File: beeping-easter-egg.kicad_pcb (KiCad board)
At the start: 2 copper layers, 9 parts, among them Q1 2N3904, SW1 SW_SPDT_312, U1 ICM7556

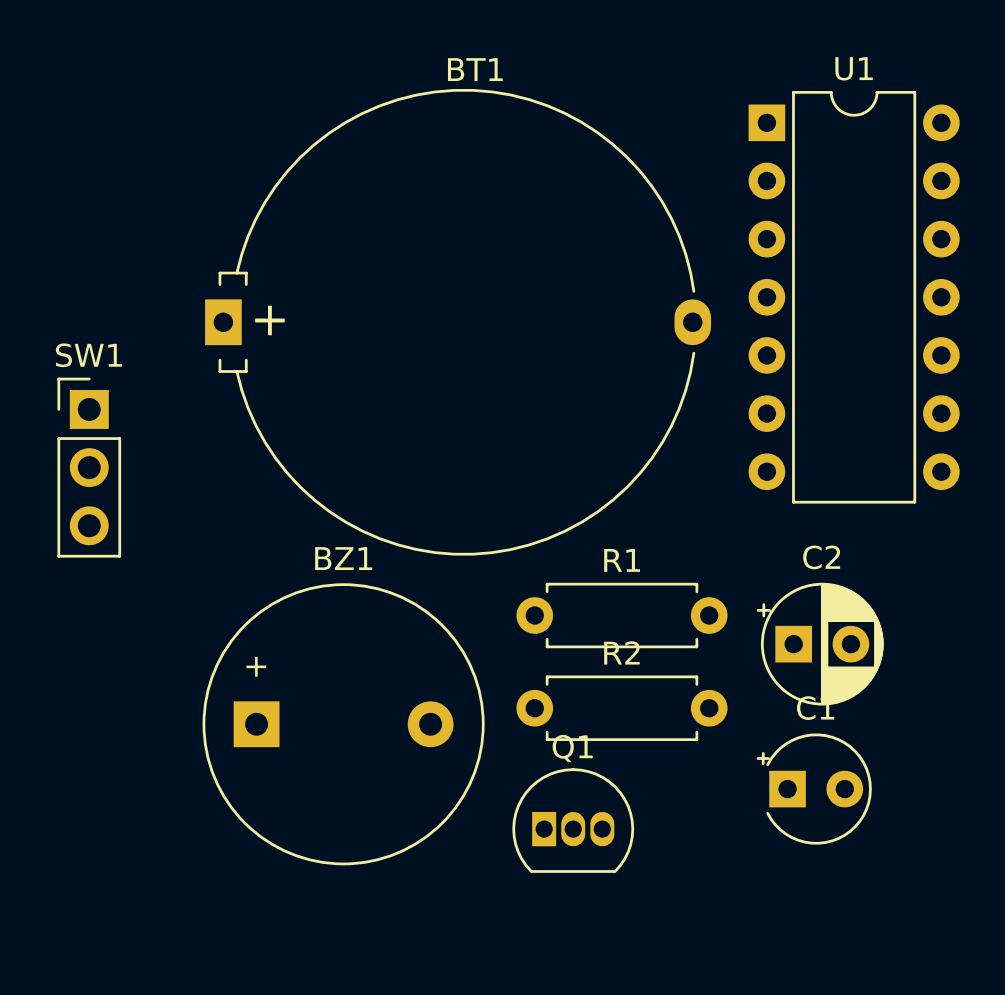
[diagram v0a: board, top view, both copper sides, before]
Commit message: update pcb from schematic
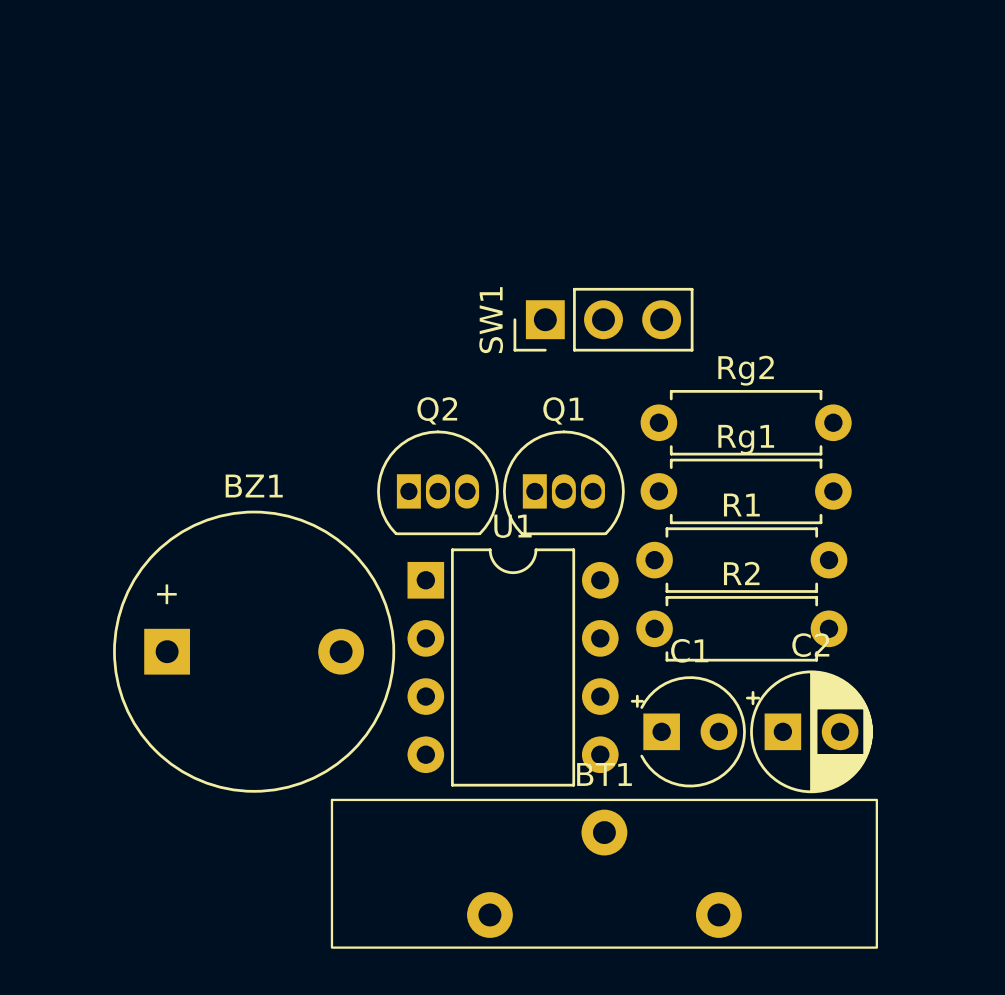
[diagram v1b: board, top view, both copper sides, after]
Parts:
- added Q2: 2N3906, Package_TO_SOT_THT:TO-92_Inline, F.Cu at (142.5, 84.0)
- added Rg1: 10kΩ, Resistor_THT:R_Axial_DIN0207_L6.3mm_D2.5mm_P7.62mm_Horizontal, F.Cu at (153.4, 84.0)
- added Rg2: 220Ω, Resistor_THT:R_Axial_DIN0207_L6.3mm_D2.5mm_P7.62mm_Horizontal, F.Cu at (153.4, 81.0)
- BT1: footprint Battery:Battery_Panasonic_CR2032-HFN_Horizontal_CircularHoles -> Library:AAA-BAT-038-K01
- C1: value C -> 10nF
- C2: value C_Polarized_US -> 0.47µF
- Q1: value 2N3904 -> 2N3906
- R1: renamed from R2; value R_US -> 510kΩ
- R2: renamed from R1; value R_US -> 1MΩ
- U1: value ICM7556 -> TLC555xP; footprint Package_DIP:DIP-14_W7.62mm -> Package_DIP:DIP-8_W7.62mm
- moved BT1 29.3 mm to (151.0, 100.7)
- moved U1 24.9 mm to (143.2, 87.9)
- moved SW1 20.3 mm to (148.4, 76.5), turned to 90 degrees
- moved Q1 14.8 mm to (148.0, 84.0)
- moved R1 8.32 mm to (153.2, 87.0)
- moved C1 6.04 mm to (153.5, 94.5)
- moved R2 5.26 mm to (153.2, 90.0)
- moved BZ1 5.03 mm to (131.9, 91.0)
- moved C2 3.86 mm to (158.8, 94.5)
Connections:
- BZ1 pad 2: Net-(BZ1--) -> Net-(BT1--)
- C1 pad 1: Net-(U1A-CV) -> Net-(U1-CV)
- C2 pad 1: Net-(U1A-THR) -> Net-(U1-THR)
- Q1 pad 1: Net-(BT1--) -> Net-(Q1-E)
- Q1 pad 3: Net-(BZ1--) -> Net-(Q1-C)
- R1 pad 1: Net-(U1A-THR) -> Net-(Q1-C)
- R1 pad 2: Net-(U1A-DIS) -> Net-(U1-DIS)
- R2 pad 1: Net-(BZ1-+) -> Net-(U1-DIS)
- R2 pad 2: Net-(U1A-DIS) -> Net-(U1-THR)
- SW1 pad 3: Net-(BZ1-+) -> Net-(Q1-E)
- U1 pad 1: Net-(U1A-DIS) -> Net-(BT1--)
- U1 pad 2: Net-(U1A-THR) -> Net-(U1-THR)
- U1 pad 3: Net-(U1A-CV) -> Net-(U1-Q)
- U1 pad 4: Net-(BZ1-+) -> Net-(Q1-C)
- U1 pad 5: Net-(U1A-Q) -> Net-(U1-CV)
- U1 pad 6: Net-(U1A-THR) -> Net-(U1-THR)
- U1 pad 7: Net-(BT1--) -> Net-(U1-DIS)
- U1 pad 8: Net-(U1A-Q) -> Net-(Q1-C)

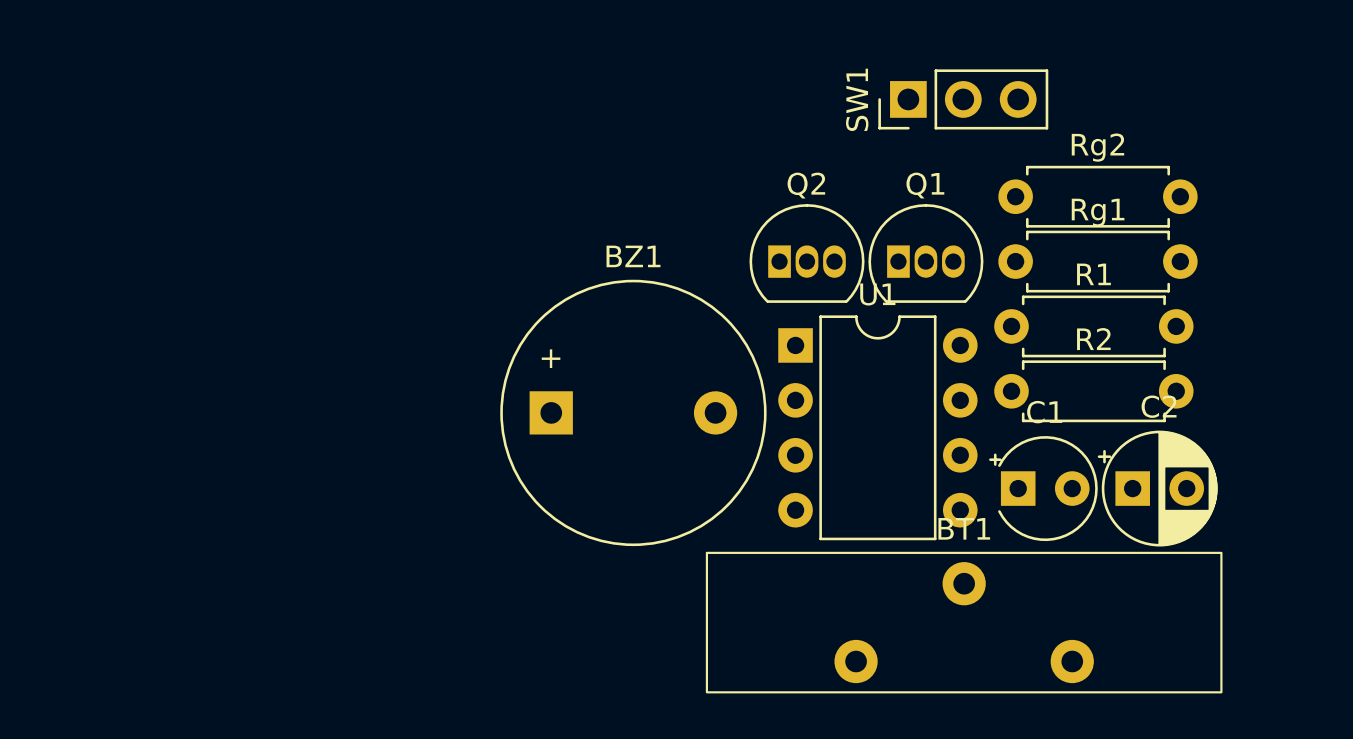
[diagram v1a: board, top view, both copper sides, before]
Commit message: switch from bjts to mosfets
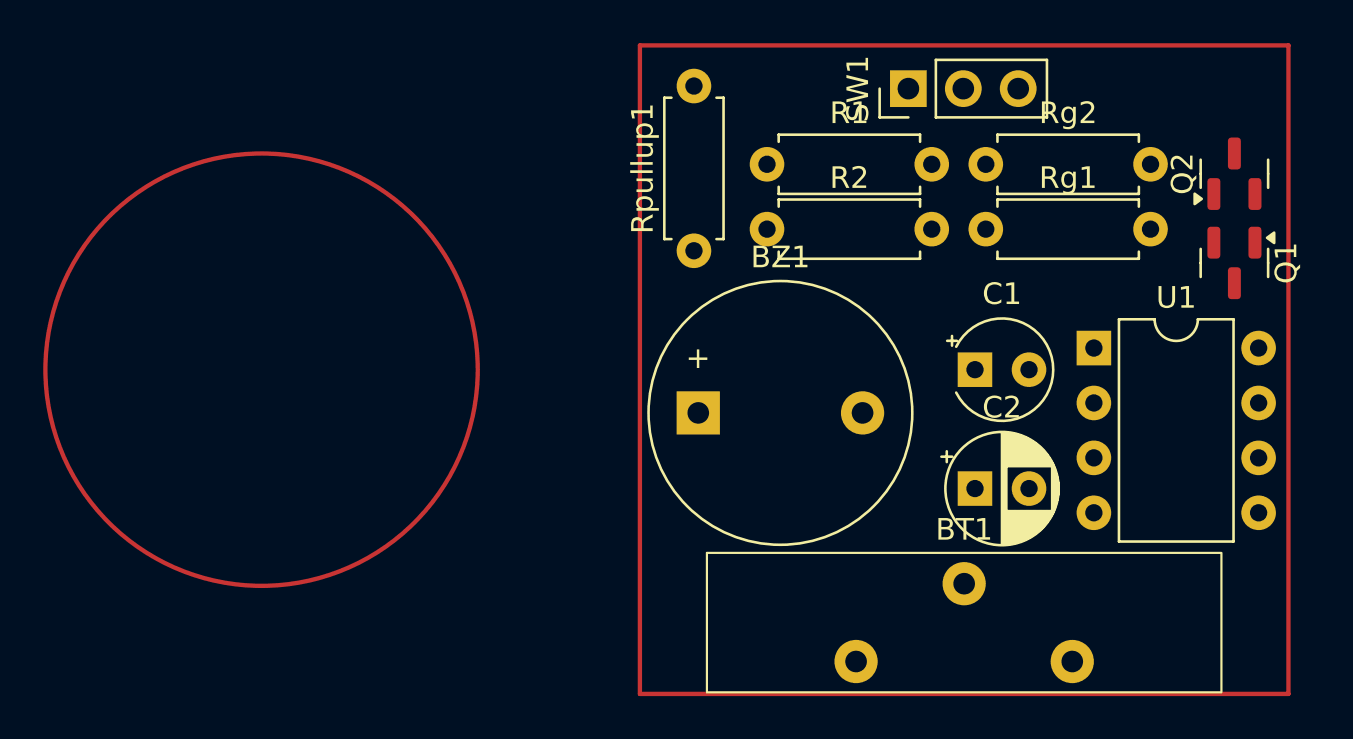
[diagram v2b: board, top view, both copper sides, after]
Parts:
- added Rpullup1: 10kΩ, Resistor_THT:R_Axial_DIN0207_L6.3mm_D2.5mm_P7.62mm_Horizontal, F.Cu at (138.5, 83.5)
- Q1, Q2: value 2N3906 -> AO3401A; footprint Package_TO_SOT_THT:TO-92_Inline -> Package_TO_SOT_SMD:SOT-23
- Rg1: value 10kΩ -> 100Ω
- Rg2: value 220Ω -> 100Ω
- moved Q2 21.4 mm to (163.5, 79.9), turned to 90 degrees
- moved Q1 15.5 mm to (163.5, 84.1), turned to -90 degrees
- moved U1 13.8 mm to (157.0, 88.0)
- moved R1 13.6 mm to (141.9, 79.5)
- moved R2 13.6 mm to (141.9, 82.5)
- moved C2 7.29 mm to (151.5, 94.5)
- moved BZ1 6.80 mm to (138.7, 91.0)
- moved C1 5.85 mm to (151.5, 89.0)
- moved Rg1 2.04 mm to (152.0, 82.5)
- moved Rg2 2.04 mm to (152.0, 79.5)
- moved SW1 0.50 mm to (148.4, 76.0)
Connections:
- Q1 pad 1: Net-(Q1-E) -> Net-(Q1-G)
- Q1 pad 2: Net-(Q1-B) -> Net-(Q1-S)
- Q1 pad 3: Net-(Q1-C) -> Net-(Q1-D)
- Q2 pad 1: Net-(Q1-C) -> Net-(Q2-G)
- Q2 pad 2: Net-(Q2-B) -> Net-(Q1-S)
- R1 pad 1: Net-(Q1-C) -> Net-(Q1-S)
- Rg1 pad 1: Net-(Q1-B) -> Net-(Q1-G)
- Rg2 pad 1: Net-(Q2-B) -> Net-(Q2-G)
- SW1 pad 3: Net-(Q1-E) -> Net-(Q1-D)
- U1 pad 4: Net-(Q1-C) -> Net-(Q1-S)
- U1 pad 8: Net-(Q1-C) -> Net-(Q1-S)

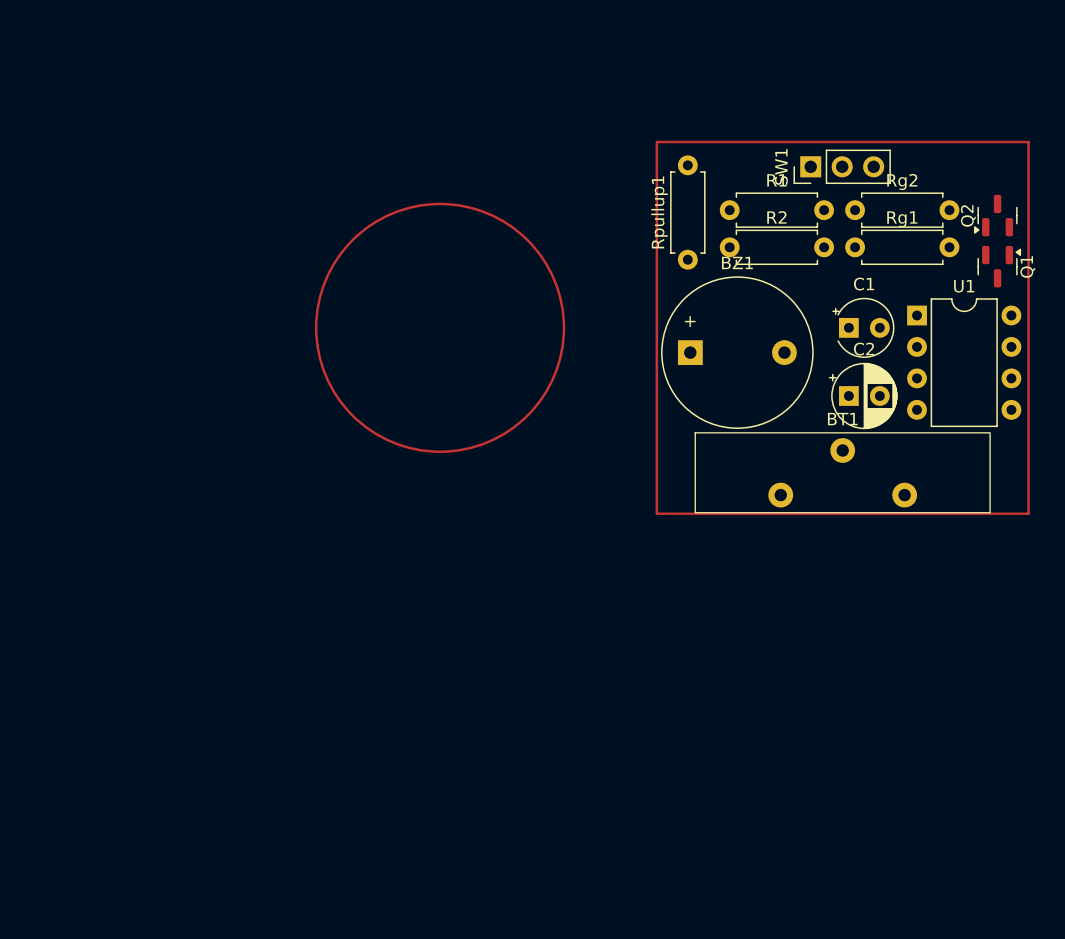
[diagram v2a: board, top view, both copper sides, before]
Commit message: Switch to SMD footprints. Add filter cap to reset.
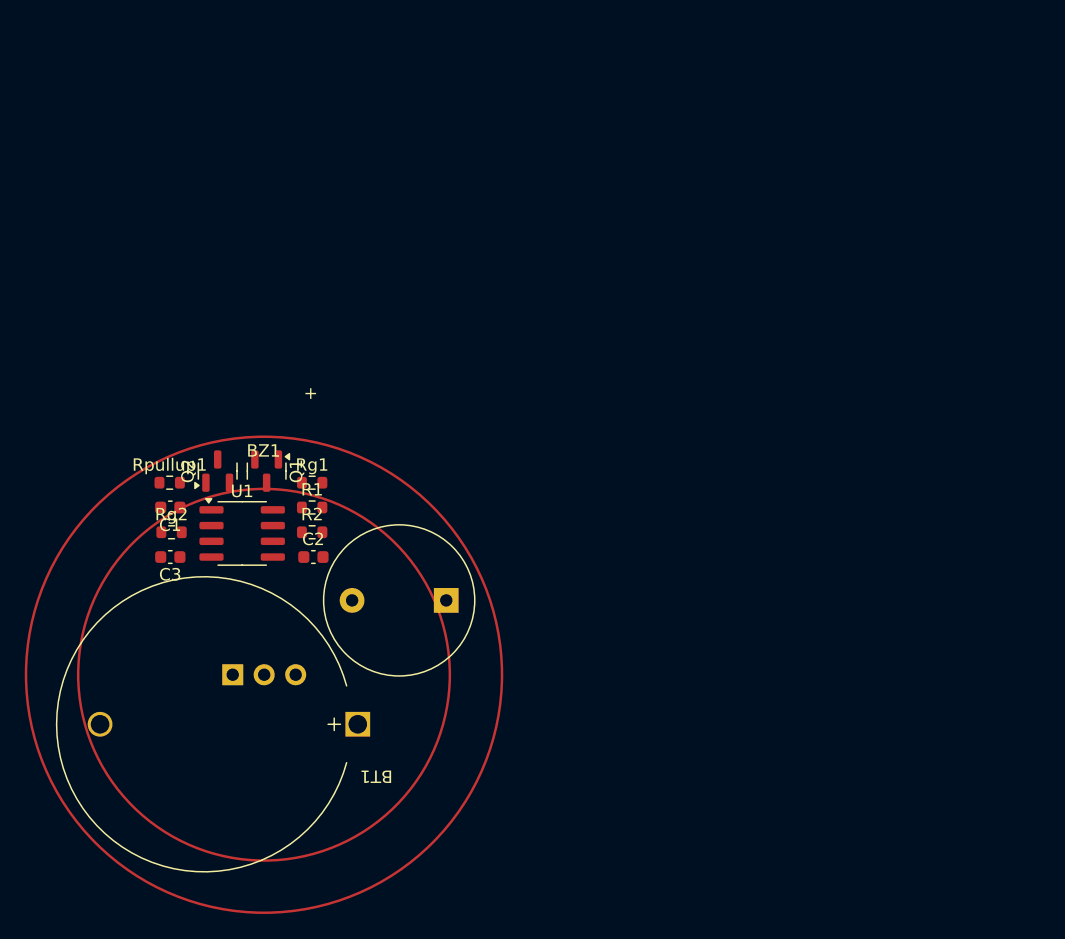
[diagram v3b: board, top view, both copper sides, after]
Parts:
- added C3: 10nF, Capacitor_SMD:C_0603_1608Metric, F.Cu at (96.7, 107.5)
- BT1: footprint Library:AAA-BAT-038-K01 -> Battery:BatteryHolder_MYOUNG_BS-07-A1BJ001_CR2032
- C1: value 10nF -> 0.47µF; footprint Capacitor_THT:CP_Radial_Tantal_D4.5mm_P2.50mm -> Capacitor_SMD:C_0603_1608Metric
- C2: value 0.47µF -> 10nF; footprint Capacitor_THT:CP_Radial_D5.0mm_P2.50mm -> Capacitor_SMD:C_0603_1608Metric
- R1, R2, Rg1, Rpullup1: footprint Resistor_THT:R_Axial_DIN0207_L6.3mm_D2.5mm_P7.62mm_Horizontal -> Resistor_SMD:R_0603_1608Metric
- Rg2: value 100Ω -> 300Ω; footprint Resistor_THT:R_Axial_DIN0207_L6.3mm_D2.5mm_P7.62mm_Horizontal -> Resistor_SMD:R_0603_1608Metric
- SW1: moved to B.Cu
- U1: footprint Package_DIP:DIP-8_W7.62mm -> Package_SO:SOIC-8_3.9x4.9mm_P1.27mm
- moved Q2 66.2 mm to (100.5, 100.6)
- moved SW1 62.1 mm to (101.8, 117.0), turned to -90 degrees
- moved Q1 61.3 mm to (104.5, 100.6)
- moved Rg2 61.0 mm to (96.8, 105.5)
- moved U1 57.2 mm to (102.5, 105.6)
- moved C1 56.7 mm to (96.7, 103.5), turned to 180 degrees
- moved Rg1 47.8 mm to (108.2, 101.5)
- moved Rpullup1 45.5 mm to (96.7, 101.5), turned to 0 degrees
- moved C2 45.1 mm to (108.3, 107.5)
- moved BT1 44.1 mm to (111.9, 121.0), turned to 180 degrees
- moved R1 41.4 mm to (108.2, 103.5)
- moved R2 40.8 mm to (108.2, 105.5)
- moved BZ1 28.1 mm to (119.0, 111.0), turned to 180 degrees
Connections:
- C1 pad 1: Net-(U1-CV) -> Net-(U1-THR)
- C2 pad 1: Net-(U1-THR) -> Net-(U1-CV)

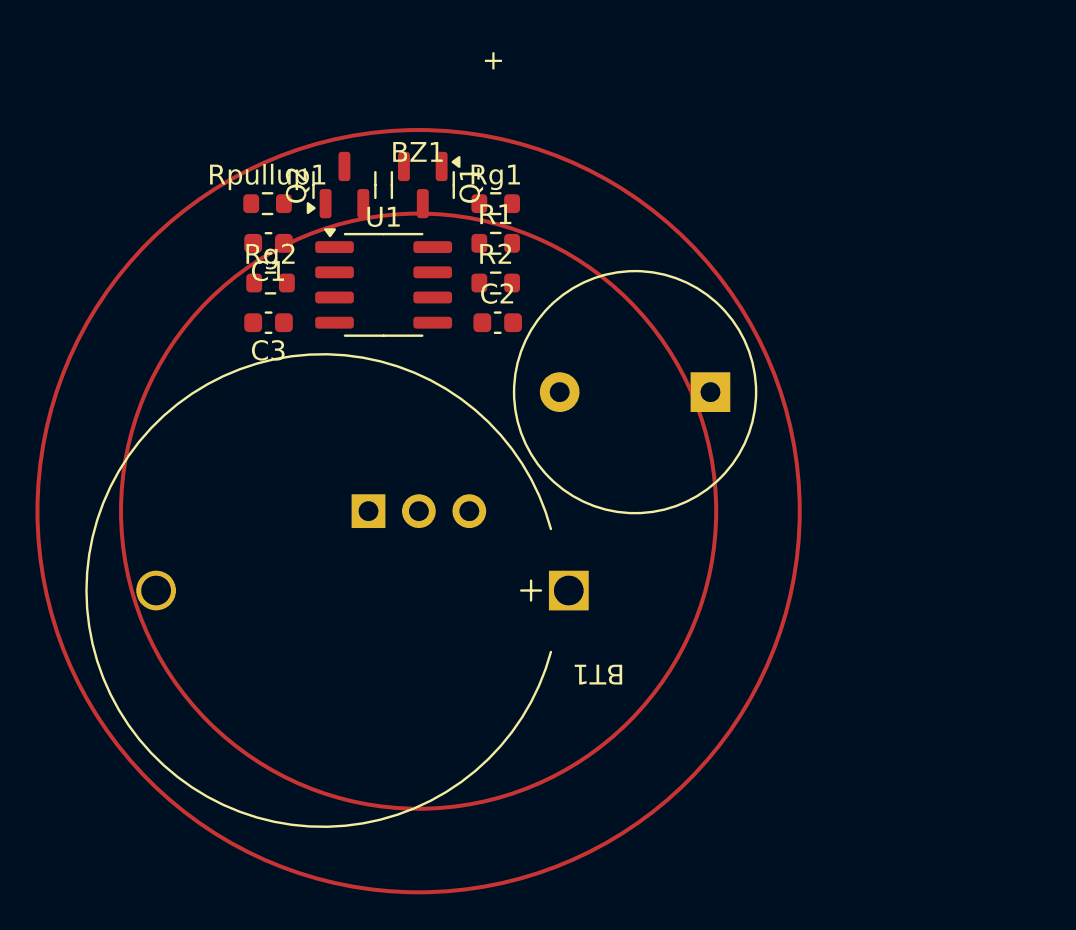
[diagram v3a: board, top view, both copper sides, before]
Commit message: Change 555 R and C values to reduce current. Ratio and thus timing stays the same. Some component renaming. Add LCSC field.
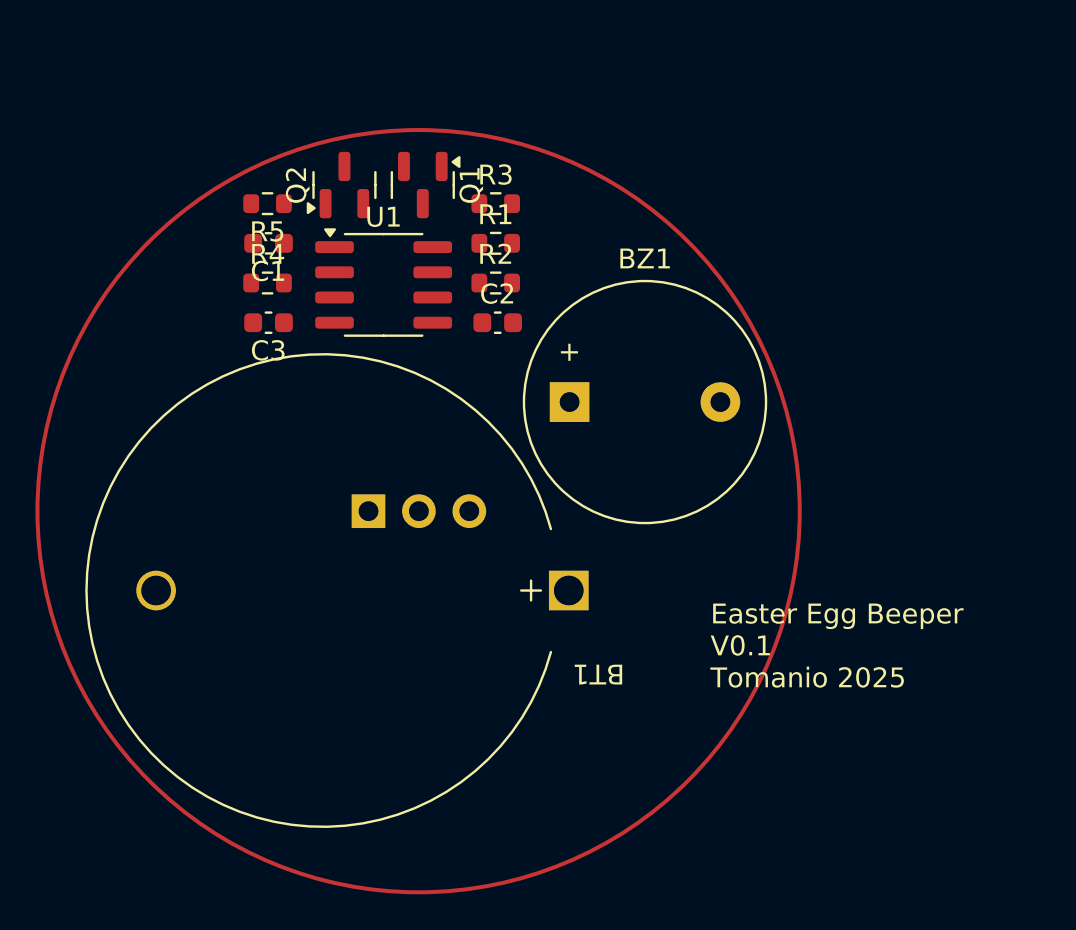
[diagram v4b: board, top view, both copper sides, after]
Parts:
- removed Rg1: 100Ω, Resistor_SMD:R_0603_1608Metric
- removed Rg2: 300Ω, Resistor_SMD:R_0603_1608Metric
- removed Rpullup1: 10kΩ, Resistor_SMD:R_0603_1608Metric
- added R3: 100Ω, Resistor_SMD:R_0603_1608Metric, F.Cu at (108.2, 101.5)
- added R4: 300Ω, Resistor_SMD:R_0603_1608Metric, F.Cu at (96.7, 105.5)
- added R5: 10kΩ, Resistor_SMD:R_0603_1608Metric, F.Cu at (96.7, 101.5)
- C1: value 0.47µF -> 0.047µF
- R1: value 510kΩ -> 5MΩ
- R2: value 1MΩ -> 10MΩ
- moved BZ1 7.12 mm to (111.9, 111.5), turned to 0 degrees
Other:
- board text added: "Easter Egg Beeper V0.1 Tomanio 2025"
